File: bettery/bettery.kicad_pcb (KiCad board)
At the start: 2 copper layers, 72.2 x 45.2 mm, 61 parts, among them Q1 WMB014N06LG4, Q2 WMB014N06LG4, Q3 SL2319A, Q4 MMBT3904, SW1 SW_Push, U1 L9961

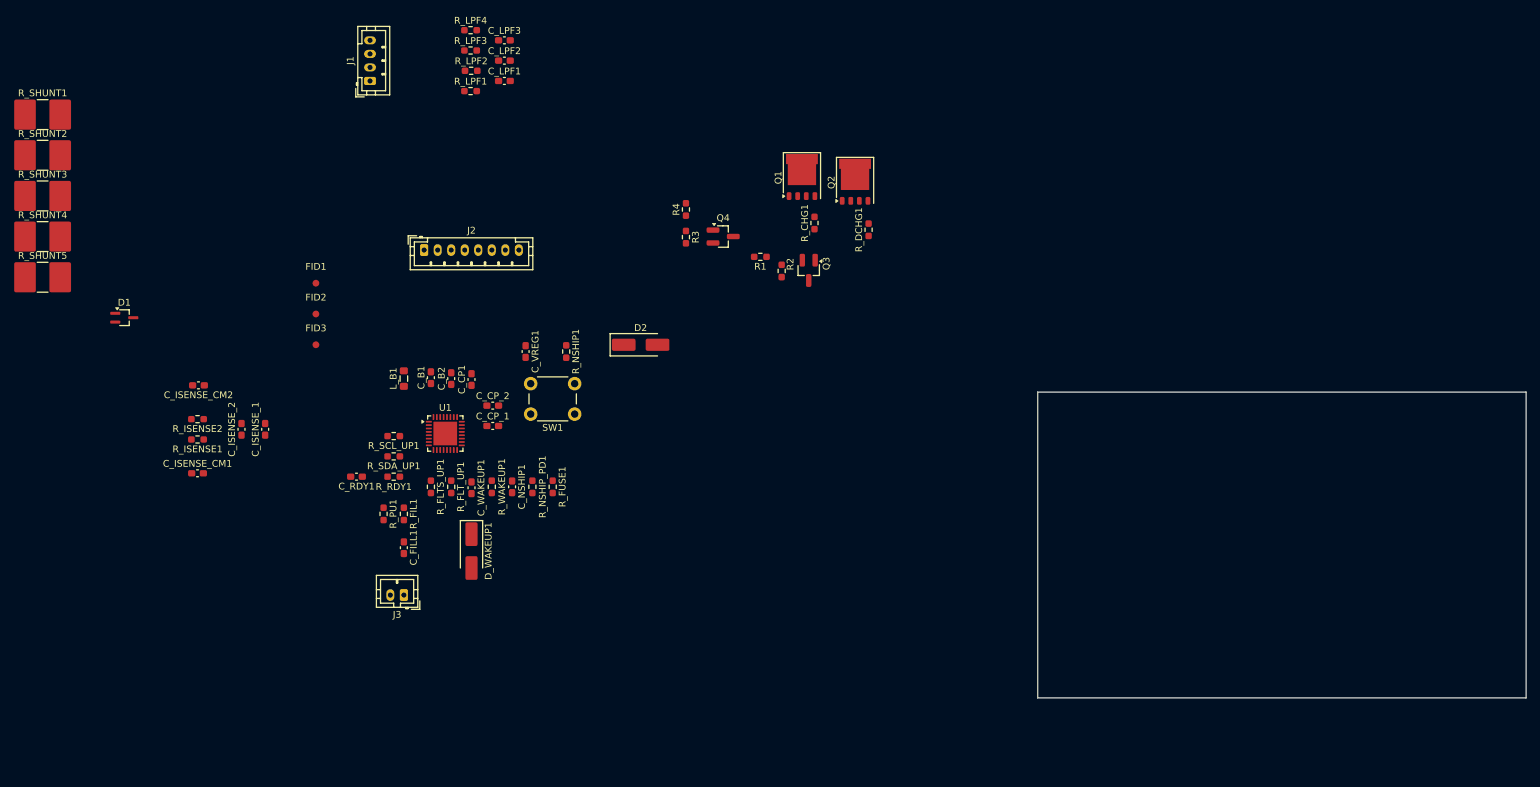
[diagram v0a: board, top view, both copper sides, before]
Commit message: complete routing
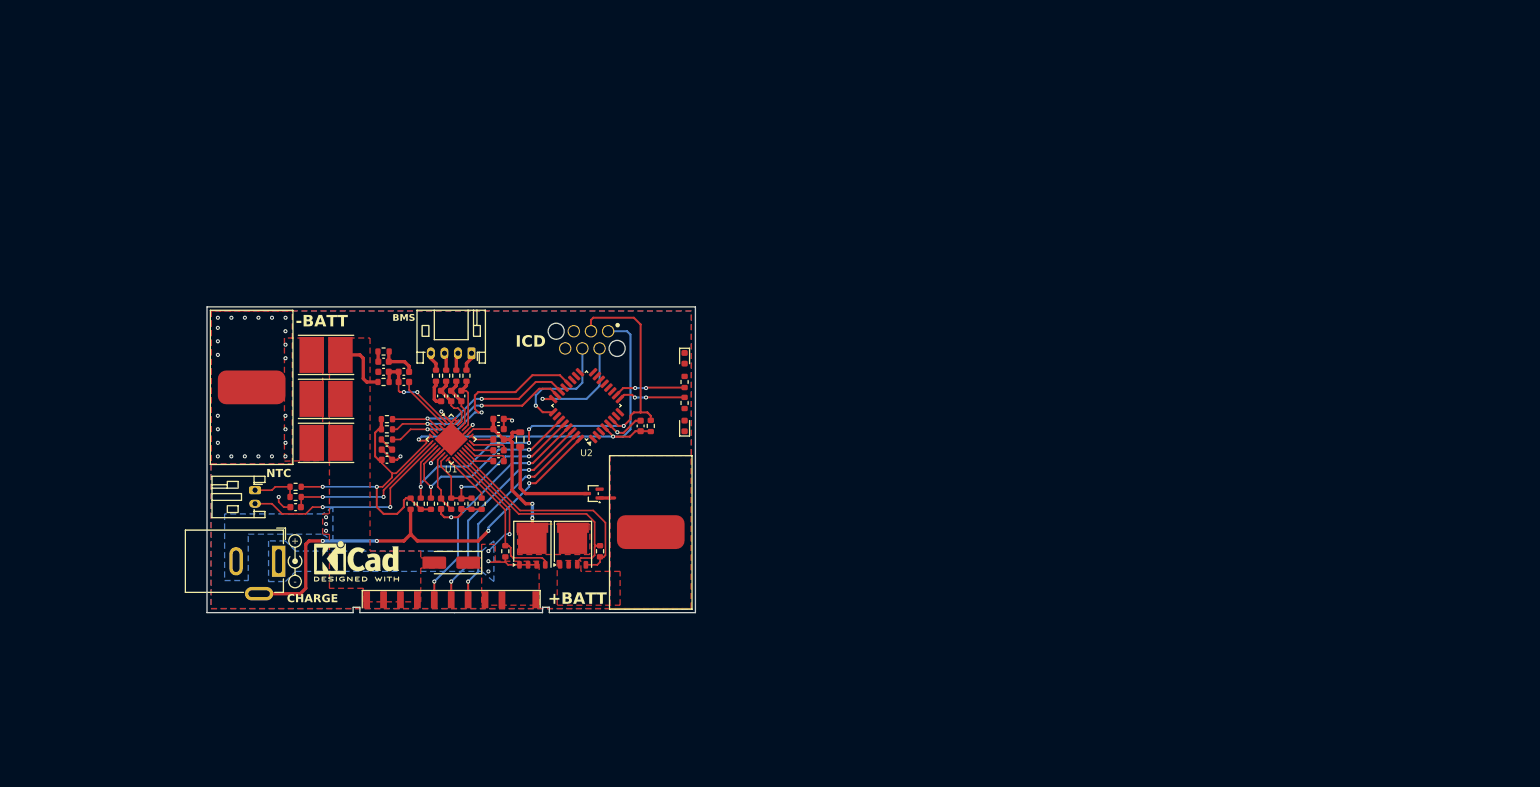
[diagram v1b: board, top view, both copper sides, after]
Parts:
- removed D_WAKEUP1: SS54, Diode_SMD:D_SMA_Handsoldering
- removed FID1, FID2, FID3: Fiducial, Fiducial:Fiducial_1mm_Mask3mm
- removed Q3: SL2319A, Package_TO_SOT_SMD:SOT-23_Handsoldering
- removed Q4: MMBT3904, Package_TO_SOT_SMD:SOT-23_Handsoldering
- removed R1: 1M, Resistor_SMD:R_0603_1608Metric_Pad0.98x0.95mm_HandSolder
- removed R2: 330k, Resistor_SMD:R_0603_1608Metric_Pad0.98x0.95mm_HandSolder
- removed R3: 47k, Resistor_SMD:R_0603_1608Metric_Pad0.98x0.95mm_HandSolder
- removed R4, R_NSHIP1: 10k, Resistor_SMD:R_0603_1608Metric_Pad0.98x0.95mm_HandSolder
- removed R_SHUNT4, R_SHUNT5: 10m, Resistor_SMD:R_2816_7142Metric_Pad3.20x4.45mm_HandSolder
- removed SW1: SW_Push, Button_Switch_THT:SW_PUSH_6mm
- added C_B3: 10u, Capacitor_SMD:C_0603_1608Metric, F.Cu at (128.0, 95.0)
- added D_LED1: LED, LED_SMD:LED_0603_1608Metric, F.Cu at (134.5, 85.0)
- added D_LED2: LED, LED_SMD:LED_0603_1608Metric, F.Cu at (134.5, 95.0)
- added H1: MountingHole_Pad, Connector_Wire:SolderWirePad_1x01_SMD_5x10mm, F.Cu at (129.5, 110.7)
- added H2: MountingHole_Pad, Connector_Wire:SolderWirePad_1x01_SMD_5x10mm, F.Cu at (70.5, 89.3)
- added J4: Conn_ARM_SWD_TagConnect_TC2030, bettery:WR-WST-REDFIT-IDC-6pin, F.Cu at (123.2, 81.0)
- added J_CHG1: Barrel_Jack_Switch, Connector_BarrelJack:BarrelJack_GCT_DCJ200-10-A_Horizontal, F.Cu at (74.5, 115.0)
- added REF**: KiCad-Logo2_5mm_SilkScreen, Symbol:KiCad-Logo2_5mm_SilkScreen, F.Cu at (86.0, 115.0)
- added REF**: Symbol_Barrel_Polarity, Symbol:Symbol_Barrel_Polarity, F.Cu at (76.8, 115.0)
- added R_LED1: 10k, Resistor_SMD:R_0603_1608Metric, F.Cu at (134.5, 88.5)
- added R_LED2: 10k, Resistor_SMD:R_0603_1608Metric, F.Cu at (134.5, 91.6)
- added R_PU2: 10k, Resistor_SMD:R_0603_1608Metric, F.Cu at (94.0, 106.5)
- added R_PU3: 10k, Resistor_SMD:R_0603_1608Metric, F.Cu at (129.5, 95.0)
- added U2: STM32G070KBTx, Package_QFP:LQFP-32_7x7mm_P0.8mm, F.Cu at (120.0, 92.0)
- C_B1, C_B2, C_CP1, C_CP_1, C_CP_2, C_FILL1, C_ISENSE_1, C_ISENSE_2, C_ISENSE_CM1, C_ISENSE_CM2, C_LPF1, C_LPF2, C_LPF3, C_NSHIP1, C_RDY1, C_VREG1, C_WAKEUP1: footprint Capacitor_SMD:C_0603_1608Metric_Pad1.08x0.95mm_HandSolder -> Capacitor_SMD:C_0603_1608Metric
- D1: footprint Package_TO_SOT_SMD:SOT-323_SC-70_Handsoldering -> Package_TO_SOT_SMD:SOT-323_SC-70
- J1: footprint Connector_JST:JST_PH_B4B-PH-K_1x04_P2.00mm_Vertical -> Connector_JST:JST_PH_S4B-PH-K_1x04_P2.00mm_Horizontal
- J2: value ~ -> Conn_01x10_Socket; footprint Connector_JST:JST_PH_B8B-PH-K_1x08_P2.00mm_Vertical -> bettery:1674231_SMD
- J3: footprint Connector_JST:JST_PH_B2B-PH-K_1x02_P2.00mm_Vertical -> Connector_JST:JST_PH_S2B-PH-K_1x02_P2.00mm_Horizontal
- L_B1: footprint Inductor_SMD:L_0805_2012Metric_Pad1.05x1.20mm_HandSolder -> Inductor_SMD:L_0805_2012Metric
- R_CHG1, R_DCHG1, R_FIL1, R_FLTS_UP1, R_FLT_UP1, R_FUSE1, R_ISENSE1, R_ISENSE2, R_LPF1, R_LPF2, R_LPF3, R_LPF4, R_NSHIP_PD1, R_PU1, R_RDY1, R_SCL_UP1, R_SDA_UP1, R_WAKEUP1: footprint Resistor_SMD:R_0603_1608Metric_Pad0.98x0.95mm_HandSolder -> Resistor_SMD:R_0603_1608Metric
- R_SHUNT1, R_SHUNT2, R_SHUNT3: value 10m -> 6m; footprint Resistor_SMD:R_2816_7142Metric_Pad3.20x4.45mm_HandSolder -> bettery:R_Shunt_Vishay_WSHP2818
- moved D1 74.0 mm to (121.0, 105.0), turned to 180 degrees
- moved Q2 71.9 mm to (112.0, 112.8)
- moved R_DCHG1 71.7 mm to (108.0, 113.5)
- moved Q1 64.2 mm to (118.0, 112.8)
- moved R_CHG1 58.0 mm to (122.0, 113.5), turned to -90 degrees
- moved R_SHUNT3 55.6 mm to (81.5, 97.5)
- moved R_SHUNT2 55.2 mm to (81.5, 91.0)
- moved R_SHUNT1 54.9 mm to (81.5, 84.5)
- moved C_LPF3 53.0 mm to (101.5, 90.6), turned to -90 degrees
- moved J2 51.9 mm to (100.0, 120.7), turned to -90 degrees
- moved R_LPF4 51.1 mm to (102.2, 87.6), turned to -90 degrees
- moved C_LPF2 50.2 mm to (100.0, 90.6), turned to -90 degrees
- moved R_LPF3 48.1 mm to (100.8, 87.6), turned to -90 degrees
- moved C_LPF1 47.5 mm to (98.5, 90.6), turned to -90 degrees
- moved R_LPF2 45.2 mm to (99.2, 87.6), turned to -90 degrees
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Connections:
- J2 pad 1: /FS -> +PACK
- J2 pad 2: /GPIO3 -> +PACK
- J2 pad 3: /FAULTN -> +PACK
- J2 pad 4: /FAULTN_SAFE -> /HOST_SDA
- J2 pad 5: /RDY -> /HOST_SCL
- J2 pad 6: /SDA -> /HOST_SMBA
- J2 pad 7: /SCL -> -PACK
- J2 pad 8: -BATT -> -PACK
- J3 pad 1: /OD -> Net-(J3-Pin_1)
- J3 pad 2: Net-(J3-Pin_2) -> /OD
- Q1 pad 2: Net-(Q1-G) -> /CHG
- R_CHG1 pad 2: Net-(Q1-G) -> /CHG
- R_FIL1 pad 2: Net-(J3-Pin_2) -> Net-(J3-Pin_1)
- R_PU1 pad 2: Net-(J3-Pin_2) -> Net-(J3-Pin_1)
- R_WAKEUP1 pad 1: /NSHIP -> /WAKEUP
- R_WAKEUP1 pad 2: /WAKEUP -> /NSHIP
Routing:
- net /VREG: track 0.00 -> 105.1 mm, vias 0 -> 4
- net /FAULTN_SAFE: track 0.00 -> 74.3 mm, vias 0 -> 4
- net /CHG_SIG: track 0.00 -> 65.8 mm, vias 0 -> 4
- net -BATT: track 0.00 -> 48.8 mm, vias 0 -> 32
- net /HOST_SMBA: track 0.00 -> 35.5 mm, vias 0 -> 2
- net +BATT: track 0.00 -> 35.5 mm
- net /RDY: track 0.00 -> 34.8 mm, vias 0 -> 2
- net /CHG: track 0.00 -> 34.2 mm
- net /HOST_SCL: track 0.00 -> 33.6 mm, vias 0 -> 2
- net /OD: track 0.00 -> 32.9 mm, vias 0 -> 2
- net /FAULTN: track 0.00 -> 31.7 mm, vias 0 -> 2
- net /HOST_SDA: track 0.00 -> 31.7 mm, vias 0 -> 2
- net /NSHIP: track 0.00 -> 30.9 mm, vias 0 -> 2
- net /SCL: track 0.00 -> 30.0 mm, vias 0 -> 2
- net /SDA: track 0.00 -> 29.1 mm, vias 0 -> 2
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- added copper zone on F.Cu, net +BATT
- added copper zone on B.Cu, net +PACK
- added copper zone on F.Cu, net +PACK
- added copper zone on B.Cu, net -BATT
- added copper zone on F.Cu, net -BATT
- added copper zone on B.Cu, net -PACK
- added copper zone on F.Cu, net -PACK
- added copper zone on F.Cu, net /VB
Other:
- outline, holes or cut-outs redrawn
- board text added: "+"
- board text added: "+BATT"
- board text added: "-"
- board text added: "-BATT"
- board text added: "BMS"
- board text added: "CHARGE"
- board text added: "ICD"
- board text added: "NTC"

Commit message: sync
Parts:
- moved C_B3 3.61 mm to (125.0, 97.0), turned to 45 degrees
- moved C_ISENSE_1 2.55 mm to (93.5, 91.0)
- moved C_ISENSE_2 2.55 mm to (93.5, 89.5)
- moved C_ISENSE_CM1 2.55 mm to (90.5, 88.0)
- moved C_ISENSE_CM2 2.55 mm to (90.5, 89.5)
- moved R_ISENSE1 2.55 mm to (90.5, 86.5)
- moved R_ISENSE2 2.55 mm to (90.5, 91.0)
- moved D2 2.20 mm to (100.0, 113.0)
- moved R_PU3 1.50 mm to (128.0, 95.0)
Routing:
- net -BATT: track 48.8 -> 54.2 mm, vias 32 -> 35
- net /VREG: track 105.1 -> 108.4 mm
- net -PACK: track 8.88 -> 6.05 mm
- net /ISENSEP: track 14.7 -> 12.4 mm
- net /ISENSEM: track 13.9 -> 11.7 mm
- net /FAULTN_SAFE: track 74.3 -> 73.1 mm
- net /CHG_SIG: track 65.8 -> 64.7 mm, vias 4 -> 5
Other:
- board text added: "LED1"
- board text added: "LED2"

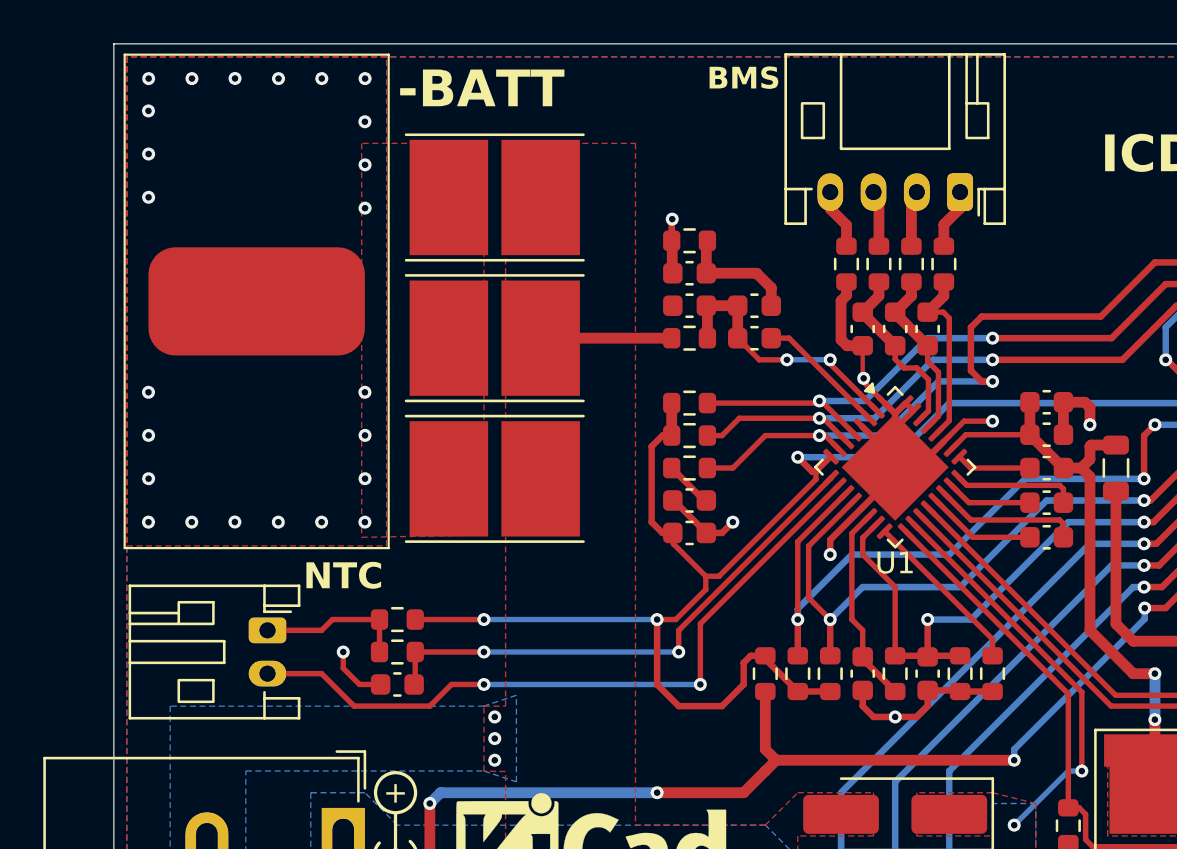
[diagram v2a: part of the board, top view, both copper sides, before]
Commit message: move ntc connector to top side of the board
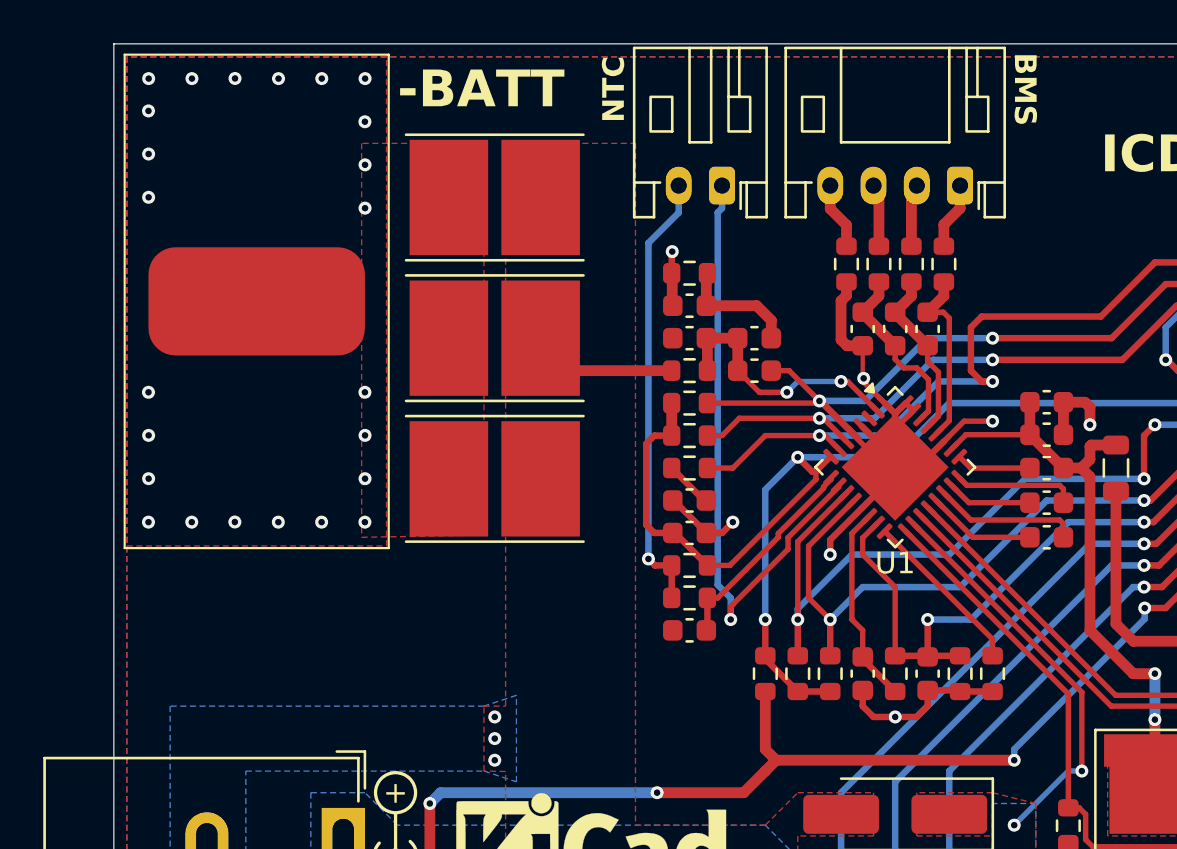
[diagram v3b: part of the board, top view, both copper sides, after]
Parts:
- moved J3 29.4 mm to (92.0, 84.0), turned to 180 degrees
- moved C_FILL1 13.7 mm to (90.5, 104.5)
- moved R_FIL1 13.7 mm to (90.5, 103.0)
- moved R_PU1 13.7 mm to (90.5, 101.5)
- moved C_ISENSE_1 1.50 mm to (93.5, 92.5)
- moved C_ISENSE_2 1.50 mm to (93.5, 91.0)
- moved C_ISENSE_CM1 1.50 mm to (90.5, 89.5)
- moved C_ISENSE_CM2 1.50 mm to (90.5, 91.0)
- moved R_ISENSE1 1.50 mm to (90.5, 88.0)
- moved R_ISENSE2 1.50 mm to (90.5, 92.5)
- moved J1 0.30 mm to (103.0, 84.0)
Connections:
- J3 pad 1: Net-(J3-Pin_1) -> /OD
- J3 pad 2: /OD -> Net-(J3-Pin_2)
- R_FIL1 pad 2: Net-(J3-Pin_1) -> Net-(J3-Pin_2)
- R_PU1 pad 2: Net-(J3-Pin_1) -> Net-(J3-Pin_2)
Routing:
- net Net-(J3-Pin_2): track 0.00 -> 20.5 mm, vias 0 -> 1
- net /NTC: track 24.7 -> 9.72 mm, vias 2 -> 0
- net /VREG: track 108.4 -> 93.5 mm, vias 4 -> 3
- net Net-(J3-Pin_1): track 6.88 -> 0.00 mm
- net /OD: track 32.9 -> 28.8 mm, vias 2 -> 1
- net -BATT: track 54.2 -> 51.4 mm, vias 35 -> 34
- net -PACK: track 6.05 -> 6.68 mm
